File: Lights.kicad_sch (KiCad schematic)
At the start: 29 parts, among them Q1 2N7002, Q2 2N7002, Q3 2N7002, Q4 2N7002, Q5 2N7002, U2 SI8261ABC-IS, U3 SI8261ABC-IS, U4 SI8261ABC-IS, U5 SI8261ABC-IS, U6 SI8261ABC-IS

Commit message: deleted 555 timer
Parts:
- renumbered Q4 to Q3, Q5 to Q4, Q3 to Q5, R24 to R16, R25 to R17, R27 to R18, R17 to R19, R26 to R20, R27 to R21, R17 to R22, R16 to R23, R22 to R24, R23 to R25, R17 to R28, R17 to R29

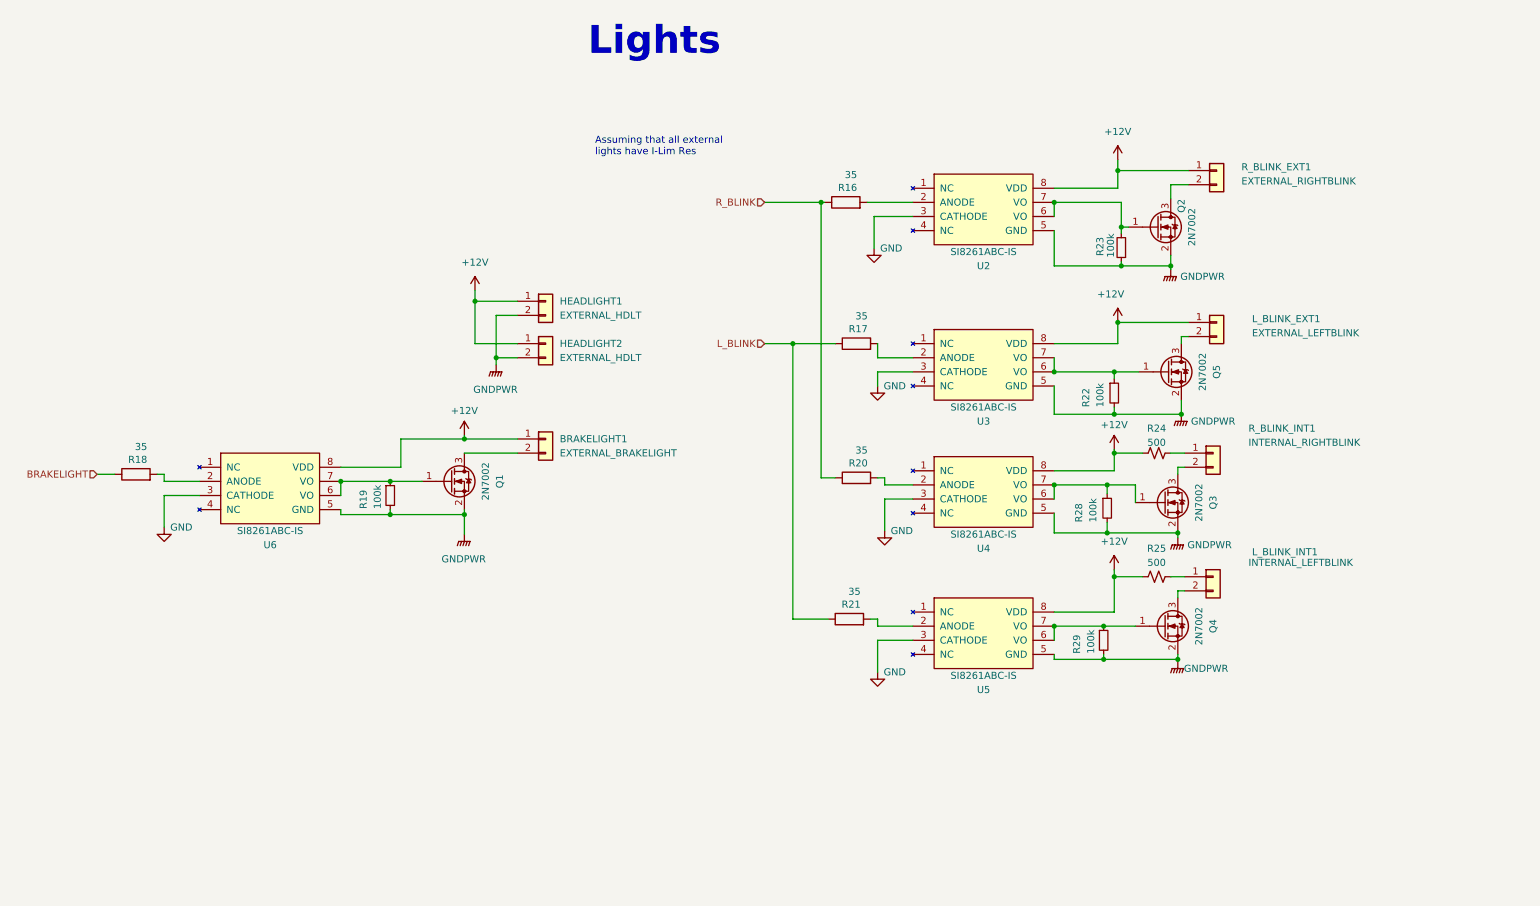
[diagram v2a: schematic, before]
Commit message: replaced gate driver and updated limiting resistor, added psom connector (made no connections yet)
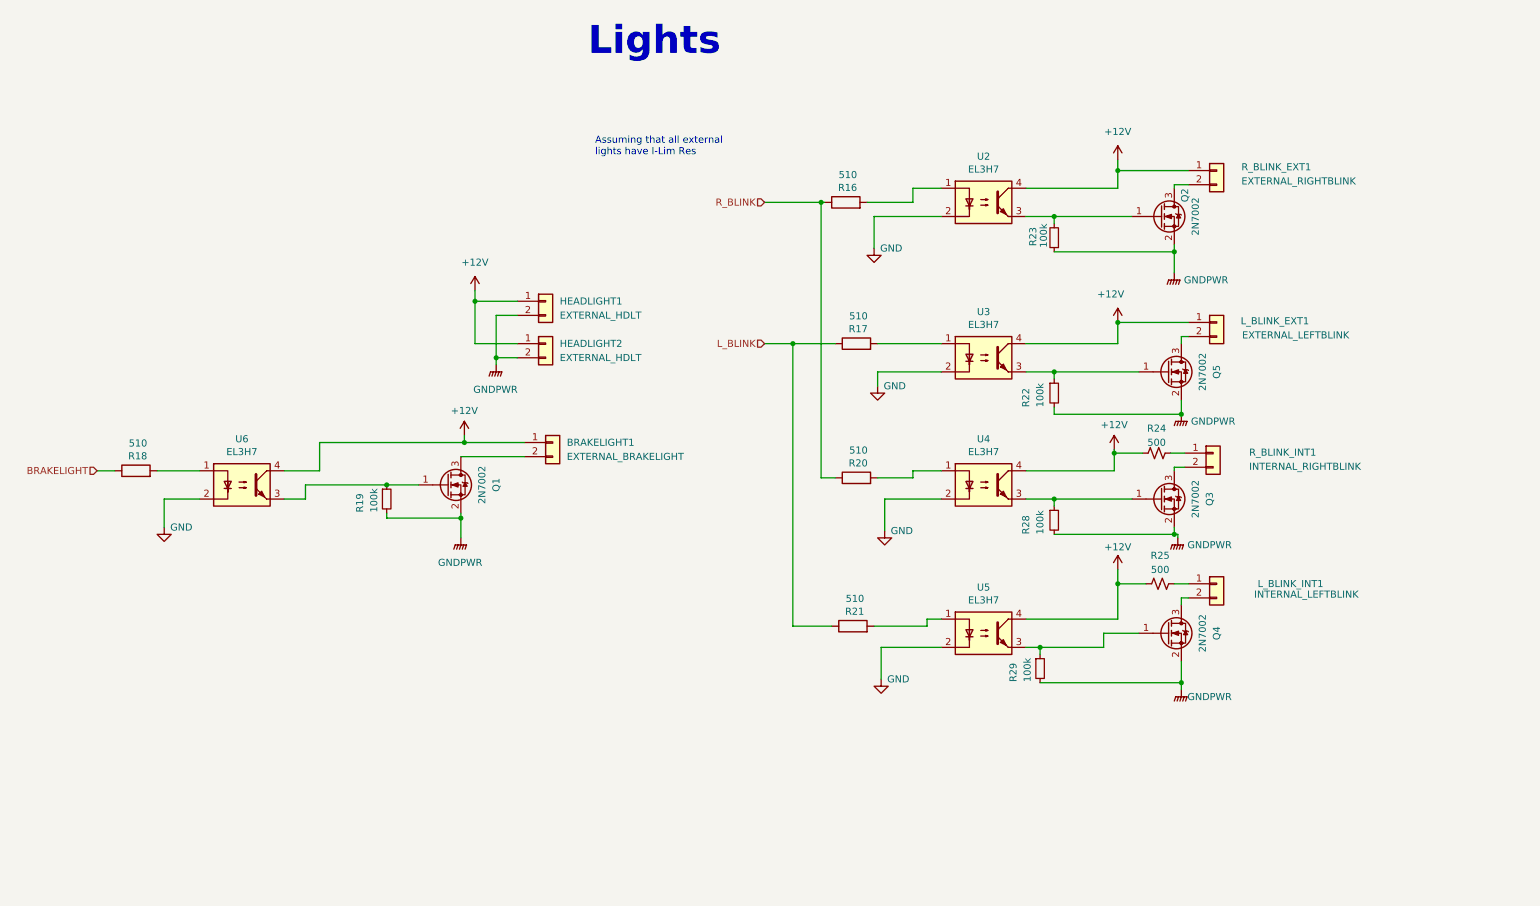
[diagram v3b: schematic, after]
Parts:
- removed U2, U3, U4, U5, U6: SI8261ABC-IS, Package_SO:SOIC-8_3.9x4.9mm_P1.27mm, symbol utsvt-bps:SI8261ABC-IS
- added U2, U3, U4, U5, U6: EL3H7, Package_DIP:DIP-4_W7.62mm, symbol Isolator:SFH617A-1
- R16, R17, R18, R20, R21: value 35 -> 510
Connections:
- net +12V: now also U2.4, U3.4, U4.4, U5.4, U6.4
- net GND: now also U2.2, U3.2, U4.2, U5.2, U6.2
- net at Q4.1 (G), R29.1: now also U5.3
- net at R21.2: now also U5.1
- net at R17.2: now also U3.1
- net at Q5.1 (G), R22.1: now also U3.3
- net at R18.2: now also U6.1
- net at Q1.1 (G), R19.1: now also U6.3
- net at Q3.1 (G), R28.1: now also U4.3
- net at R16.2: now also U2.1
- net at R20.2: now also U4.1
- net at Q2.1 (G), R23.2: now also U2.3
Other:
- moved on the sheet: BRAKELIGHT1, L_BLINK_INT1, Q1, Q2, Q3, Q4, R18, R19, R21, R22, R23, R25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

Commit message: got rid of headlights and brakelights, adjusted pinout to include just two connectors to two lights
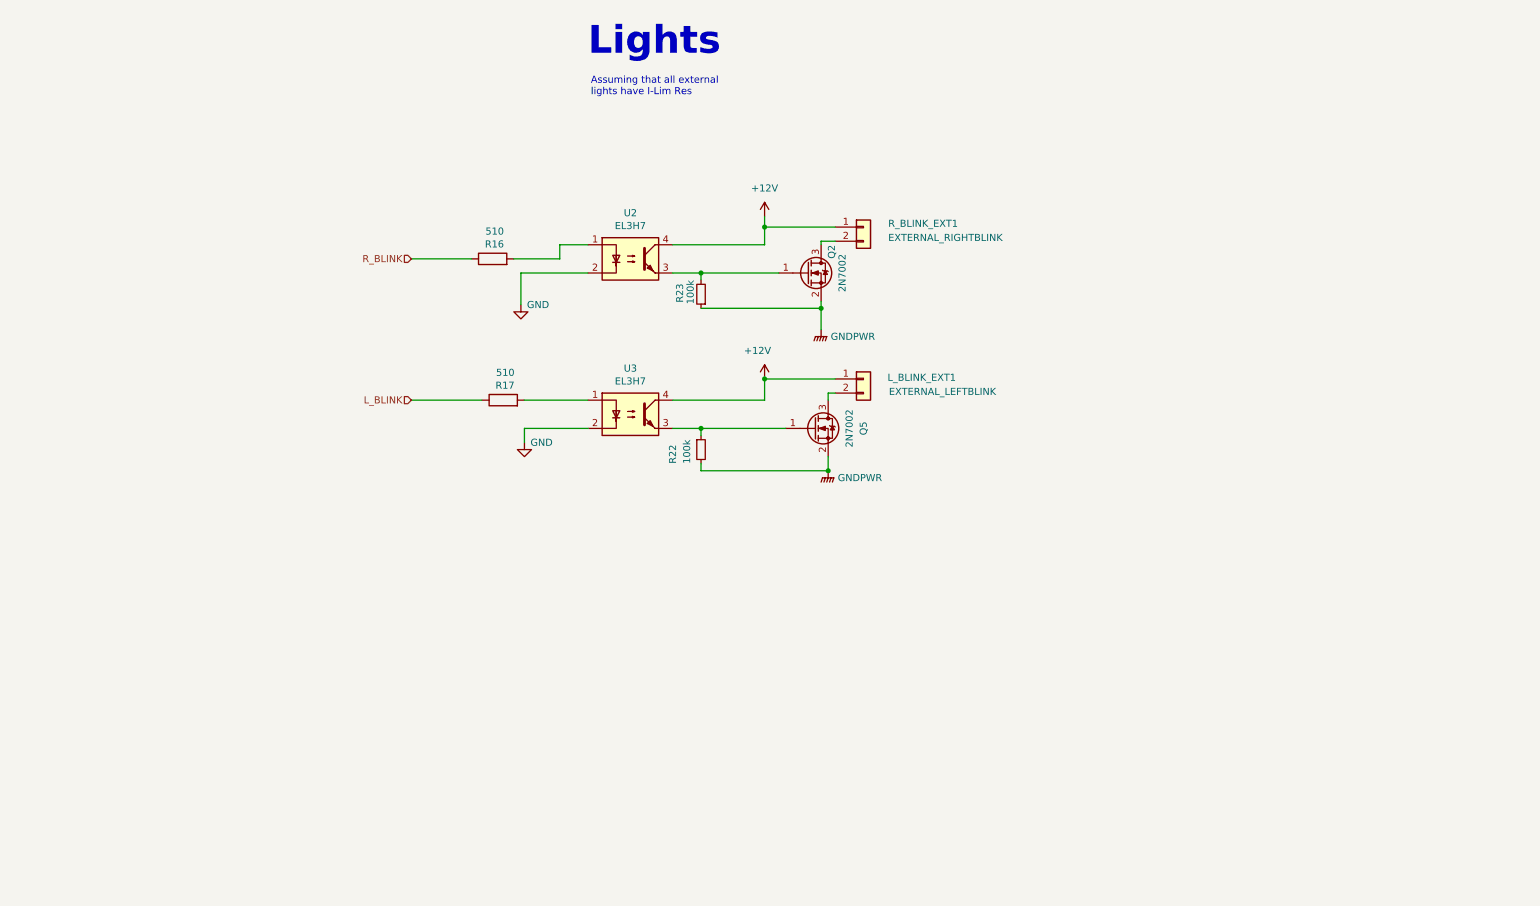
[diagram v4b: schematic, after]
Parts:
- removed BRAKELIGHT1: EXTERNAL_BRAKELIGHT, Connector_Molex:Molex_Micro-Fit_3.0_43650-0215_1x02_P3.00mm_Vertical, symbol Connector_Generic:Conn_01x02
- removed HEADLIGHT1, HEADLIGHT2: EXTERNAL_HDLT, Connector_Molex:Molex_Micro-Fit_3.0_43650-0215_1x02_P3.00mm_Vertical, symbol Connector_Generic:Conn_01x02
- removed L_BLINK_INT1: INTERNAL_LEFTBLINK, Connector_Molex:Molex_Micro-Fit_3.0_43650-0215_1x02_P3.00mm_Vertical, symbol Connector_Generic:Conn_01x02
- removed Q1, Q3, Q4: 2N7002, Package_TO_SOT_SMD:SOT-23, symbol Transistor_FET:2N7002
- removed R18, R20, R21: 510, Resistor_SMD:R_0805_2012Metric, symbol Device:R
- removed R19, R28, R29: 100k, Resistor_SMD:R_0805_2012Metric, symbol Device:R_Small
- removed R24, R25: 500, Resistor_SMD:R_0805_2012Metric, symbol Device:R_Small_US
- removed R_BLINK_INT1: INTERNAL_RIGHTBLINK, Connector_Molex:Molex_Micro-Fit_3.0_43650-0215_1x02_P3.00mm_Vertical, symbol Connector_Generic:Conn_01x02
- removed U4, U5, U6: EL3H7, Package_DIP:DIP-4_W7.62mm, symbol Isolator:SFH617A-1
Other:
- moved on the sheet: L_BLINK_EXT1, Q2, Q5, R16, R17, R22, R23, R_BLINK_EXT1, U2, U3

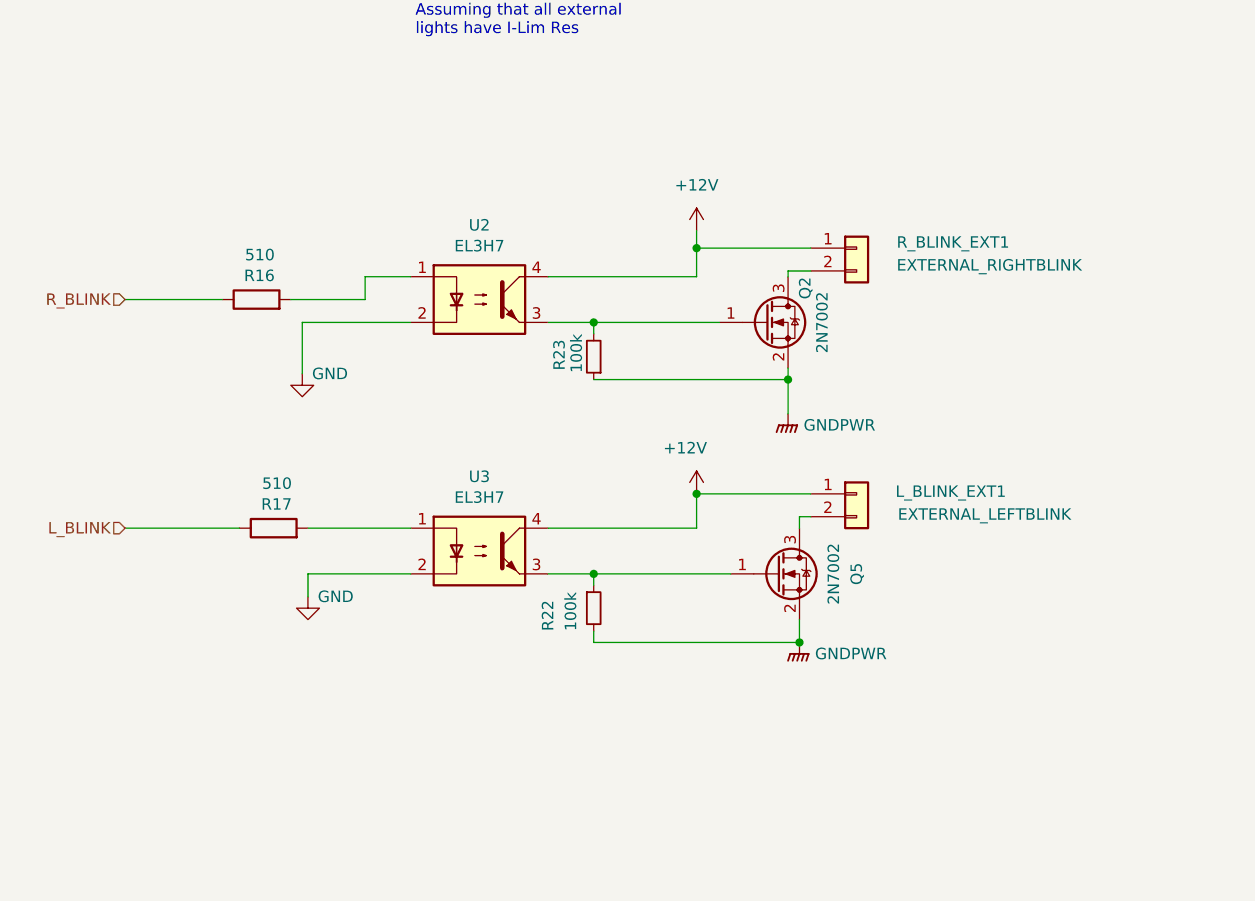
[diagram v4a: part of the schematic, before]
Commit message: added two more light connectors to board
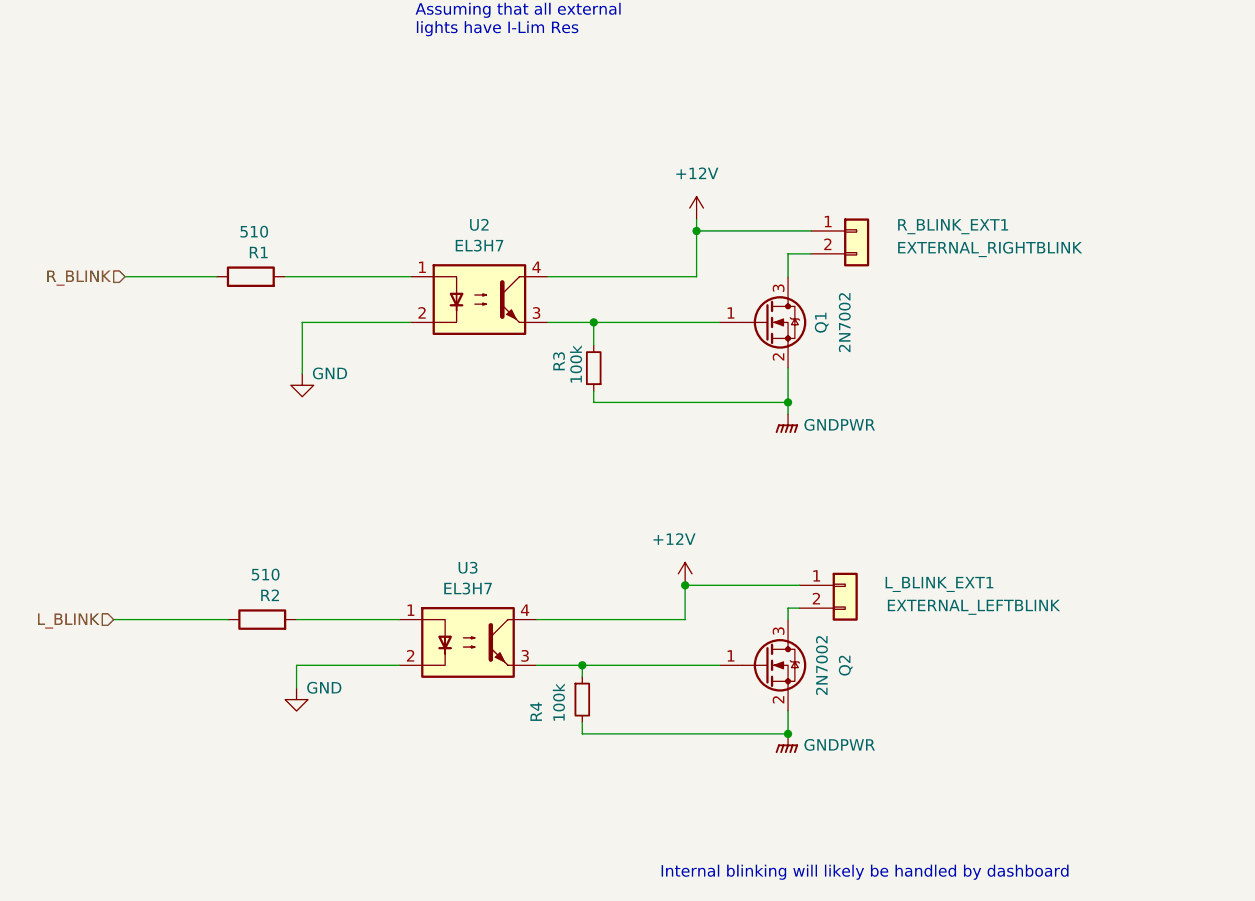
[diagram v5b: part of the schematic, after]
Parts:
- renumbered Q2 to Q1, Q5 to Q2, R16 to R1, R17 to R2, R23 to R3, R22 to R4
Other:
- note added: "Internal blinking will likely be handled by dashboard"
- moved on the sheet: L_BLINK_EXT1, Q2, R1, R2, R3, R4, R_BLINK_EXT1, U3
